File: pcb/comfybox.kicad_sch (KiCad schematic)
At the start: 19 parts

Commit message: fix option button schema
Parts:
- OPT1, OPT2, OPT3, OPT4, OPT5: footprint (none) -> Button_Switch_THT:SW_PUSH_6mm
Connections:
- net HOME: now also OPT3.1
- net L3: now also OPT5.1
- net LEFT: no longer OPT1.1, OPT2.1, OPT3.1, OPT4.1, OPT5.1
- net R3: now also OPT4.1
- net SELECT: now also OPT2.1
- net START: now also OPT1.1
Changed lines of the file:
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@@
     (stroke (width 0) (type default) (color 0 0 0 0))
   )
-  (global_label "LEFT" (shape input) (at 115.57 38.1 270) (fields_autoplaced)
-    (effects (font (size 1.27 1.27)) (justify right))
-    (property "Intersheet References" "${INTERSHEET_REFS}" (id 0) (at 115.4906 44.7464 90)
+  (global_label "START" (shape input) (at 115.57 38.1 270) (fields_autoplaced)
+    (effects (font (size 1.27 1.27)) (justify right))
+    (property "Intersheet References" "${INTERSHEET_REFS}" (id 0) (at 115.4906 46.0164 90)
       (effects (font (size 1.27 1.27)) (justify right) hide)
     )
@@
     )
   )
-  (global_label "LEFT" (shape input) (at 156.21 38.1 270) (fields_autoplaced)
-    (effects (font (size 1.27 1.27)) (justify right))
-    (property "Intersheet References" "${INTERSHEET_REFS}" (id 0) (at 156.1306 44.7464 90)
+  (global_label "HOME" (shape input) (at 156.21 38.1 270) (fields_autoplaced)
+    (effects (font (size 1.27 1.27)) (justify right))
+    (property "Intersheet References" "${INTERSHEET_REFS}" (id 0) (at 156.1306 45.7745 90)
       (effects (font (size 1.27 1.27)) (justify right) hide)
     )
@@
     )
   )
-  (global_label "LEFT" (shape input) (at 176.53 38.1 270) (fields_autoplaced)
-    (effects (font (size 1.27 1.27)) (justify right))
-    (property "Intersheet References" "${INTERSHEET_REFS}" (id 0) (at 176.4506 44.7464 90)
+  (global_label "R3" (shape input) (at 176.53 38.1 270) (fields_autoplaced)
+    (effects (font (size 1.27 1.27)) (justify right))
+    (property "Intersheet References" "${INTERSHEET_REFS}" (id 0) (at 176.4506 42.9926 90)
       (effects (font (size 1.27 1.27)) (justify right) hide)
     )
@@
     )
   )
-  (global_label "LEFT" (shape input) (at 135.89 38.1 270) (fields_autoplaced)
-    (effects (font (size 1.27 1.27)) (justify right))
-    (property "Intersheet References" "${INTERSHEET_REFS}" (id 0) (at 135.8106 44.7464 90)
+  (global_label "SELECT" (shape input) (at 135.89 38.1 270) (fields_autoplaced)
+    (effects (font (size 1.27 1.27)) (justify right))
+    (property "Intersheet References" "${INTERSHEET_REFS}" (id 0) (at 135.8106 47.2864 90)
       (effects (font (size 1.27 1.27)) (justify right) hide)
     )
@@
     )
   )
-  (global_label "LEFT" (shape input) (at 196.85 38.1 270) (fields_autoplaced)
-    (effects (font (size 1.27 1.27)) (justify right))
-    (property "Intersheet References" "${INTERSHEET_REFS}" (id 0) (at 196.7706 44.7464 90)
+  (global_label "L3" (shape input) (at 196.85 38.1 270) (fields_autoplaced)
+    (effects (font (size 1.27 1.27)) (justify right))
+    (property "Intersheet References" "${INTERSHEET_REFS}" (id 0) (at 196.7706 42.7507 90)
       (effects (font (size 1.27 1.27)) (justify right) hide)
     )
@@
     (property "Reference" "OPT5" (id 0) (at 201.93 30.48 0))
     (property "Value" "SW_Push" (id 1) (at 201.93 33.02 0))
-    (property "Footprint" "" (id 2) (at 201.93 33.02 0)
+    (property "Footprint" "Button_Switch_THT:SW_PUSH_6mm" (id 2) (at 201.93 33.02 0)
       (effects (font (size 1.27 1.27)) hide)
     )
@@
     (property "Reference" "OPT2" (id 0) (at 140.97 30.48 0))
     (property "Value" "SW_Push" (id 1) (at 140.97 33.02 0))
-    (property "Footprint" "" (id 2) (at 140.97 33.02 0)
+    (property "Footprint" "Button_Switch_THT:SW_PUSH_6mm" (id 2) (at 140.97 33.02 0)
       (effects (font (size 1.27 1.27)) hide)
     )
@@
     (property "Reference" "OPT3" (id 0) (at 161.29 30.48 0))
     (property "Value" "SW_Push" (id 1) (at 161.29 33.02 0))
-    (property "Footprint" "" (id 2) (at 161.29 33.02 0)
+    (property "Footprint" "Button_Switch_THT:SW_PUSH_6mm" (id 2) (at 161.29 33.02 0)
       (effects (font (size 1.27 1.27)) hide)
     )
@@
     (property "Reference" "OPT1" (id 0) (at 120.65 30.48 0))
     (property "Value" "SW_Push" (id 1) (at 120.65 33.02 0))
-    (property "Footprint" "" (id 2) (at 120.65 33.02 0)
+    (property "Footprint" "Button_Switch_THT:SW_PUSH_6mm" (id 2) (at 120.65 33.02 0)
       (effects (font (size 1.27 1.27)) hide)
     )
@@
     (property "Reference" "OPT4" (id 0) (at 181.61 30.48 0))
     (property "Value" "SW_Push" (id 1) (at 181.61 33.02 0))
-    (property "Footprint" "" (id 2) (at 181.61 33.02 0)
+    (property "Footprint" "Button_Switch_THT:SW_PUSH_6mm" (id 2) (at 181.61 33.02 0)
       (effects (font (size 1.27 1.27)) hide)
     )
@@
     )
     (path "/67799ff0-1f81-4b52-92af-6bd82ed8650e"
-      (reference "OPT1") (unit 1) (value "SW_Push") (footprint "")
+      (reference "OPT1") (unit 1) (value "SW_Push") (footprint "Button_Switch_THT:SW_PUSH_6mm")
     )
     (path "/65dd1a47-52fc-45ea-a616-0664e2ea6a57"
-      (reference "OPT2") (unit 1) (value "SW_Push") (footprint "")
+      (reference "OPT2") (unit 1) (value "SW_Push") (footprint "Button_Switch_THT:SW_PUSH_6mm")
     )
     (path "/66eee54a-044d-4735-8c7e-22a81e9b5f4a"
-      (reference "OPT3") (unit 1) (value "SW_Push") (footprint "")
+      (reference "OPT3") (unit 1) (value "SW_Push") (footprint "Button_Switch_THT:SW_PUSH_6mm")
     )
     (path "/f2ca8c9a-937a-4c90-92c8-28b1c0ec0147"
-      (reference "OPT4") (unit 1) (value "SW_Push") (footprint "")
+      (reference "OPT4") (unit 1) (value "SW_Push") (footprint "Button_Switch_THT:SW_PUSH_6mm")
     )
     (path "/5f4369f3-2990-462b-a6f3-e1403088f05d"
-      (reference "OPT5") (unit 1) (value "SW_Push") (footprint "")
+      (reference "OPT5") (unit 1) (value "SW_Push") (footprint "Button_Switch_THT:SW_PUSH_6mm")
     )
     (path "/1c88fcf1-197e-4669-a023-1e1afa0350b1"

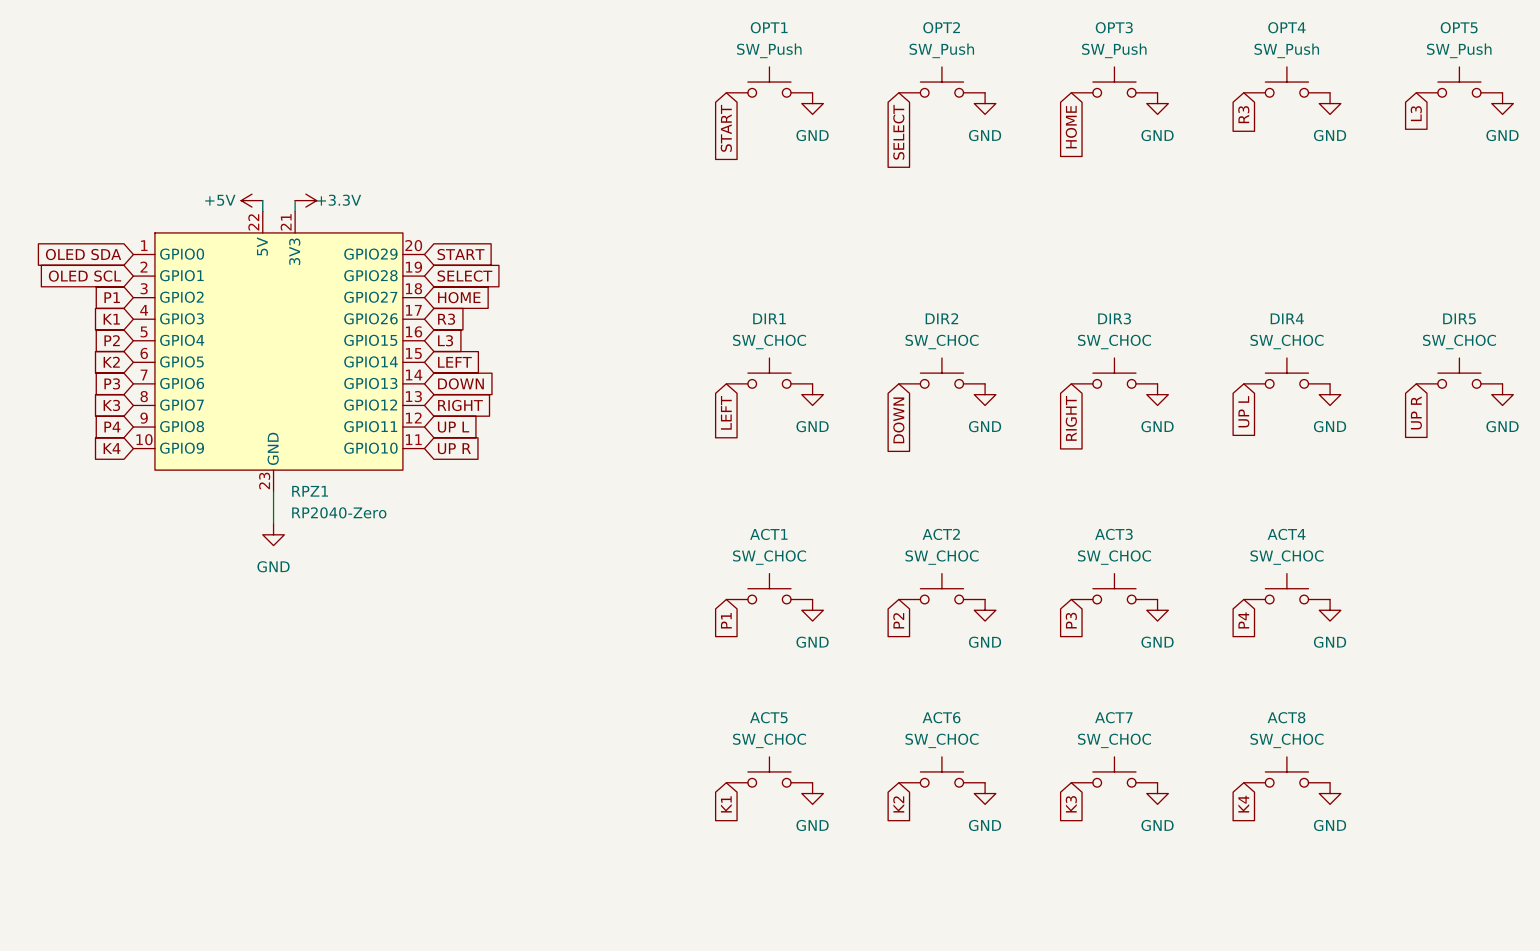
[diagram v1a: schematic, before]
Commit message: finished pcb without oled
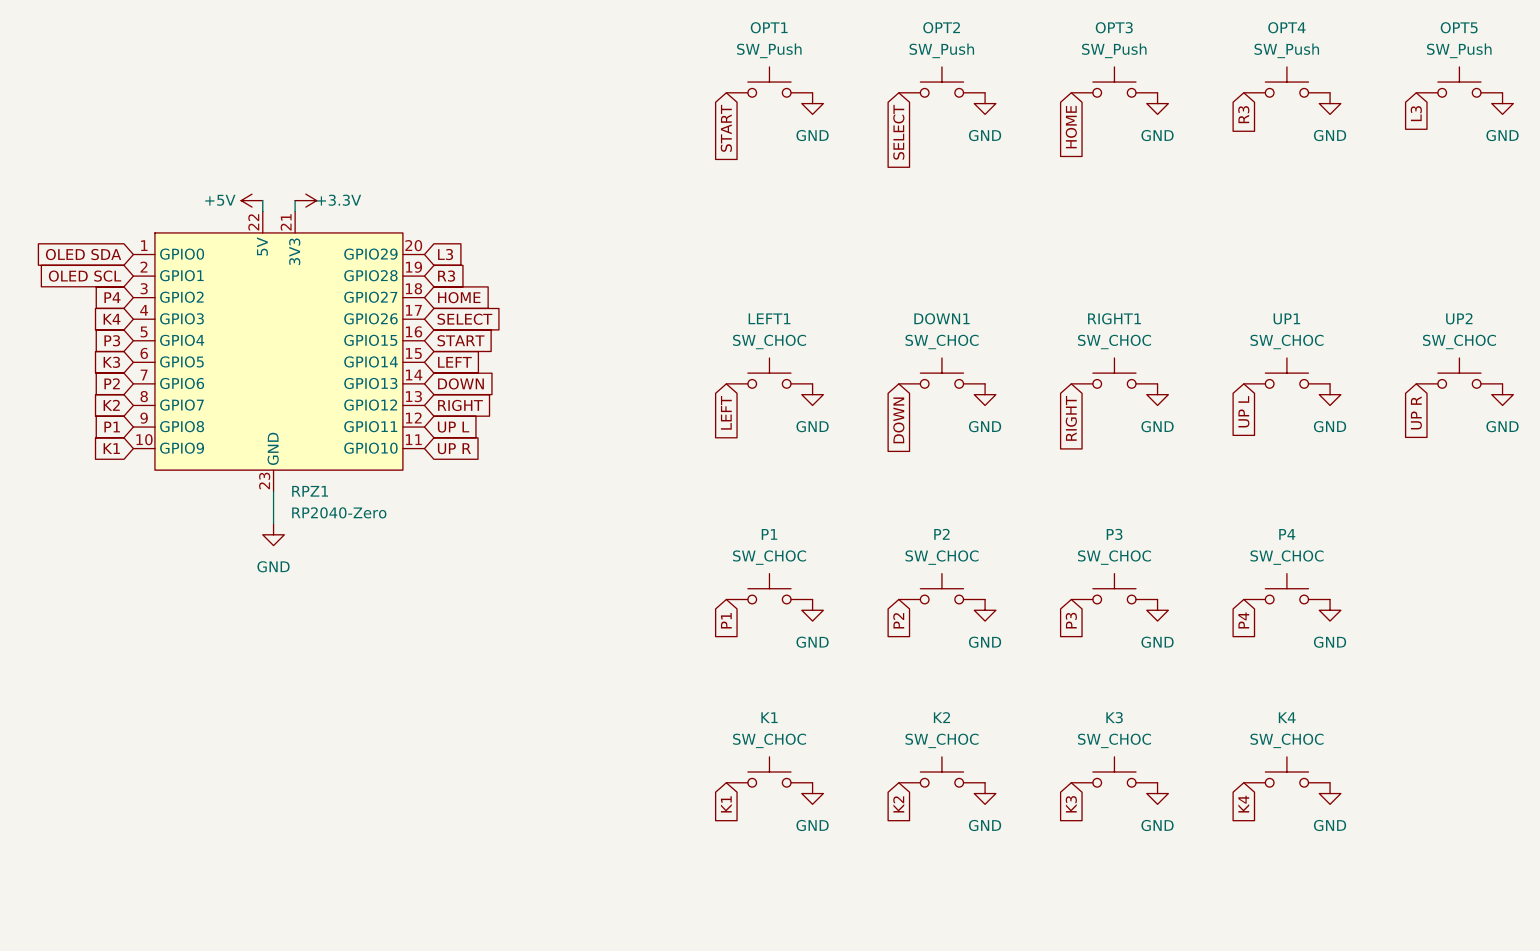
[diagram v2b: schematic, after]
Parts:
- renumbered DIR2 to DOWN1, ACT5 to K1, ACT6 to K2, ACT7 to K3, ACT8 to K4, DIR1 to LEFT1, ACT1 to P1, ACT2 to P2, ACT3 to P3, ACT4 to P4, DIR3 to RIGHT1, DIR4 to UP1, DIR5 to UP2
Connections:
- net K1: now also RPZ1.10 (GPIO9); no longer RPZ1.4 (GPIO3)
- net K2: now also RPZ1.8 (GPIO7); no longer RPZ1.6 (GPIO5)
- net K3: now also RPZ1.6 (GPIO5); no longer RPZ1.8 (GPIO7)
- net K4: now also RPZ1.4 (GPIO3); no longer RPZ1.10 (GPIO9)
- net L3: now also RPZ1.20 (GPIO29); no longer RPZ1.16 (GPIO15)
- net P1: now also RPZ1.9 (GPIO8); no longer RPZ1.3 (GPIO2)
- net P2: now also RPZ1.7 (GPIO6); no longer RPZ1.5 (GPIO4)
- net P3: now also RPZ1.5 (GPIO4); no longer RPZ1.7 (GPIO6)
- net P4: now also RPZ1.3 (GPIO2); no longer RPZ1.9 (GPIO8)
- net R3: now also RPZ1.19 (GPIO28); no longer RPZ1.17 (GPIO26)
- net SELECT: now also RPZ1.17 (GPIO26); no longer RPZ1.19 (GPIO28)
- net START: now also RPZ1.16 (GPIO15); no longer RPZ1.20 (GPIO29)

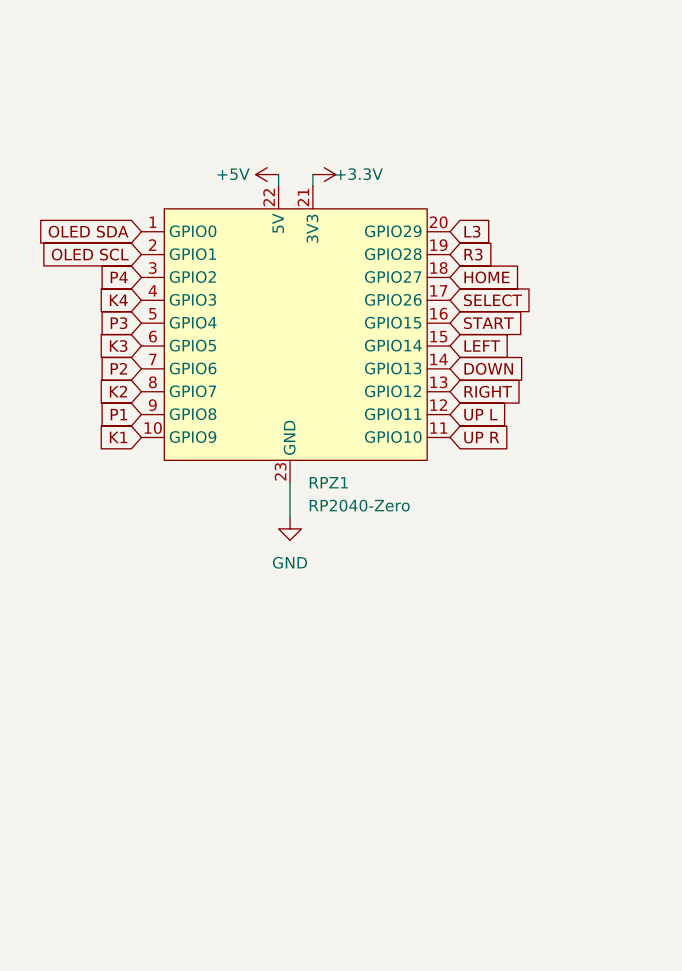
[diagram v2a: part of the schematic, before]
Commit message: add oled
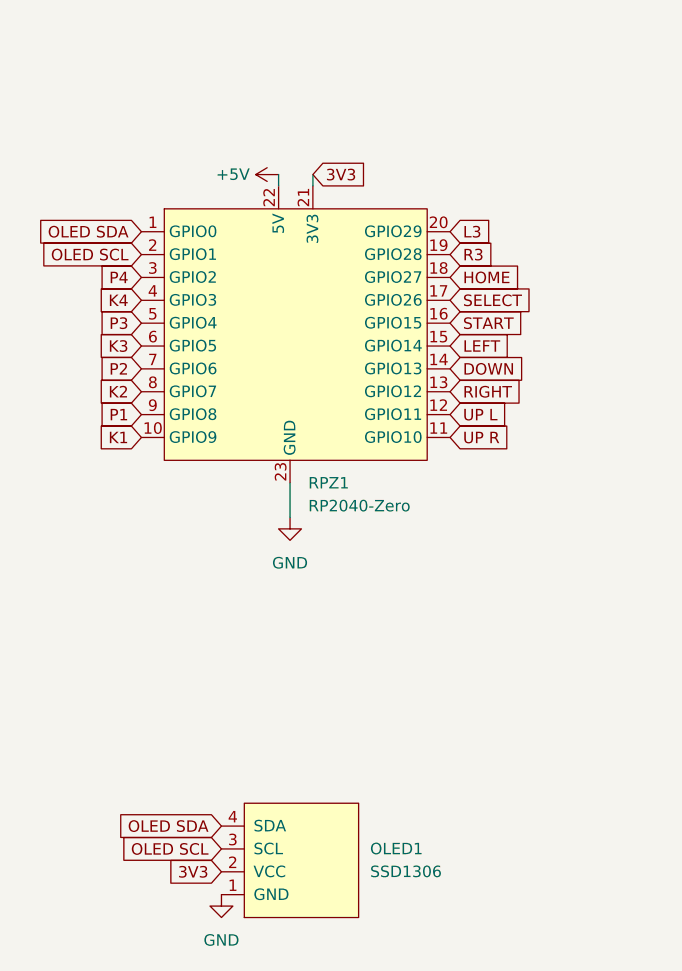
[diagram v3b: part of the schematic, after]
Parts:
- added OLED1: SSD1306, SSD1306:128x64OLED, symbol SSD1306-128x64_OLED:SSD1306
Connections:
- net GND: now also OLED1.1 (GND)
- net OLED SCL: now also OLED1.3 (SCL)
- net OLED SDA: now also OLED1.4 (SDA)
- net +3.3V renamed 3V3
- net 3V3: now also OLED1.2 (VCC)
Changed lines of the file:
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@@
+    )
+  )
+  (global_label "3V3" (shape input) (at 64.77 50.8 0) (fields_autoplaced)
+    (effects (font (size 1.27 1.27)) (justify left))
+    (property "Intersheet References" "${INTERSHEET_REFS}" (id 0) (at 70.6907 50.7206 0)
+      (effects (font (size 1.27 1.27)) (justify left) hide)
     )
   )
@@
     )
   )
+  (global_label "3V3" (shape input) (at 54.61 128.27 180) (fields_autoplaced)
+    (effects (font (size 1.27 1.27)) (justify right))
+    (property "Intersheet References" "${INTERSHEET_REFS}" (id 0) (at 48.6893 128.3494 0)
+      (effects (font (size 1.27 1.27)) (justify right) hide)
+    )
+  )
   (global_label "P4" (shape input) (at 176.53 97.79 270) (fields_autoplaced)
     (effects (font (size 1.27 1.27)) (justify right))
@@
     (effects (font (size 1.27 1.27)) (justify right))
     (property "Intersheet References" "${INTERSHEET_REFS}" (id 0) (at 40.8274 64.6906 0)
+      (effects (font (size 1.27 1.27)) (justify right) hide)
+    )
+  )
+  (global_label "OLED SDA" (shape input) (at 54.61 123.19 180) (fields_autoplaced)
+    (effects (font (size 1.27 1.27)) (justify right))
+    (property "Intersheet References" "${INTERSHEET_REFS}" (id 0) (at 42.8836 123.1106 0)
       (effects (font (size 1.27 1.27)) (justify right) hide)
     )
@@
     (effects (font (size 1.27 1.27)) (justify right))
     (property "Intersheet References" "${INTERSHEET_REFS}" (id 0) (at 135.8106 47.2864 90)
+      (effects (font (size 1.27 1.27)) (justify right) hide)
+    )
+  )
+  (global_label "OLED SCL" (shape input) (at 54.61 125.73 180) (fields_autoplaced)
+    (effects (font (size 1.27 1.27)) (justify right))
+    (property "Intersheet References" "${INTERSHEET_REFS}" (id 0) (at 42.944 125.6506 0)
       (effects (font (size 1.27 1.27)) (justify right) hide)
     )
@@
     (pin "2")
   )
+  (symbol (lib_id "SSD1306-128x64_OLED:SSD1306") (at 63.5 127 90) (unit 1)
+    (in_bom yes) (on_board yes) (fields_autoplaced)
+    (property "Reference" "OLED1" (id 0) (at 71.12 125.7299 90)
+      (effects (font (size 1.27 1.27)) (justify right))
+    )
+    (property "Value" "SSD1306" (id 1) (at 71.12 128.2699 90)
+      (effects (font (size 1.27 1.27)) (justify right))
+    )
+    (property "Footprint" "SSD1306:128x64OLED" (id 2) (at 57.15 127 0)
+      (effects (font (size 1.27 1.27)) hide)
+    )
+    (property "Datasheet" "" (id 3) (at 57.15 127 0)
+      (effects (font (size 1.27 1.27)) hide)
+    )
+    (pin "1")
+    (pin "2")
+    (pin "3")
+    (pin "4")
+  )
   (symbol (lib_id "power:GND") (at 166.37 72.39 0) (unit 1)
     (in_bom yes) (on_board yes) (fields_autoplaced)
@@
     )
     (property "Datasheet" "" (id 3) (at 207.01 38.1 0)
+      (effects (font (size 1.27 1.27)) hide)
+    )
+    (pin "1")
+  )
+  (symbol (lib_id "power:GND") (at 54.61 130.81 0) (unit 1)
+    (in_bom yes) (on_board yes) (fields_autoplaced)
+    (property "Reference" "#PWR?" (id 0) (at 54.61 137.16 0)
+      (effects (font (size 1.27 1.27)) hide)
+    )
+    (property "Value" "GND" (id 1) (at 54.61 135.89 0))
+    (property "Footprint" "" (id 2) (at 54.61 130.81 0)
+      (effects (font (size 1.27 1.27)) hide)
+    )
+    (property "Datasheet" "" (id 3) (at 54.61 130.81 0)
       (effects (font (size 1.27 1.27)) hide)
     )
@@
     (pin "1")
   )
-  (symbol (lib_id "power:+3.3V") (at 64.77 50.8 270) (unit 1)
-    (in_bom yes) (on_board yes)
-    (property "Reference" "#PWR03" (id 0) (at 60.96 50.8 0)
-      (effects (font (size 1.27 1.27)) hide)
-    )
-    (property "Value" "+3.3V" (id 1) (at 69.85 50.8 90))
-    (property "Footprint" "" (id 2) (at 64.77 50.8 0)
-      (effects (font (size 1.27 1.27)) hide)
-    )
-    (property "Datasheet" "" (id 3) (at 64.77 50.8 0)
-      (effects (font (size 1.27 1.27)) hide)
-    )
-    (pin "1")
-  )
   (symbol (lib_id "power:GND") (at 166.37 119.38 0) (unit 1)
     (in_bom yes) (on_board yes) (fields_autoplaced)
@@
       (reference "#PWR02") (unit 1) (value "GND") (footprint "")
     )
-    (path "/b0507ad9-25e2-47fa-90d4-ecb6403eeeac"
-      (reference "#PWR03") (unit 1) (value "+3.3V") (footprint "")
-    )
     (path "/9f534cec-d5b5-4308-b3e5-aa8c6eda6219"
       (reference "#PWR04") (unit 1) (value "GND") (footprint "")
@@
       (reference "#PWR021") (unit 1) (value "GND") (footprint "")
     )
+    (path "/8ebb64d1-1b87-45bc-8a21-f86410e35966"
+      (reference "#PWR?") (unit 1) (value "GND") (footprint "")
+    )
     (path "/7d452c23-f08c-4cf7-8335-8028ad6af654"
       (reference "DOWN1") (unit 1) (value "SW_CHOC") (footprint "Kailh:Kailh_socket_PG1350_optional")
@@
       (reference "LEFT1") (unit 1) (value "SW_CHOC") (footprint "Kailh:Kailh_socket_PG1350_optional")
     )
+    (path "/85c97a58-edb1-46c2-952a-8c8e5519c14c"
+      (reference "OLED1") (unit 1) (value "SSD1306") (footprint "SSD1306:128x64OLED")
+    )
     (path "/67799ff0-1f81-4b52-92af-6bd82ed8650e"
